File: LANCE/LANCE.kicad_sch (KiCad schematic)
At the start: 59 parts, among them J1 4s Batt, J12 Sparkmax 1 Pwr, J13 Lin Actuator 1 (Large), J15 Lasers, J16 SHT30, J17 Lin Actuator 2 (Small), J19 Sparkmax PWM 1, J2 12V, J20 Sparkmax PWM 2, J21 Sparkmax 2 Pwr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

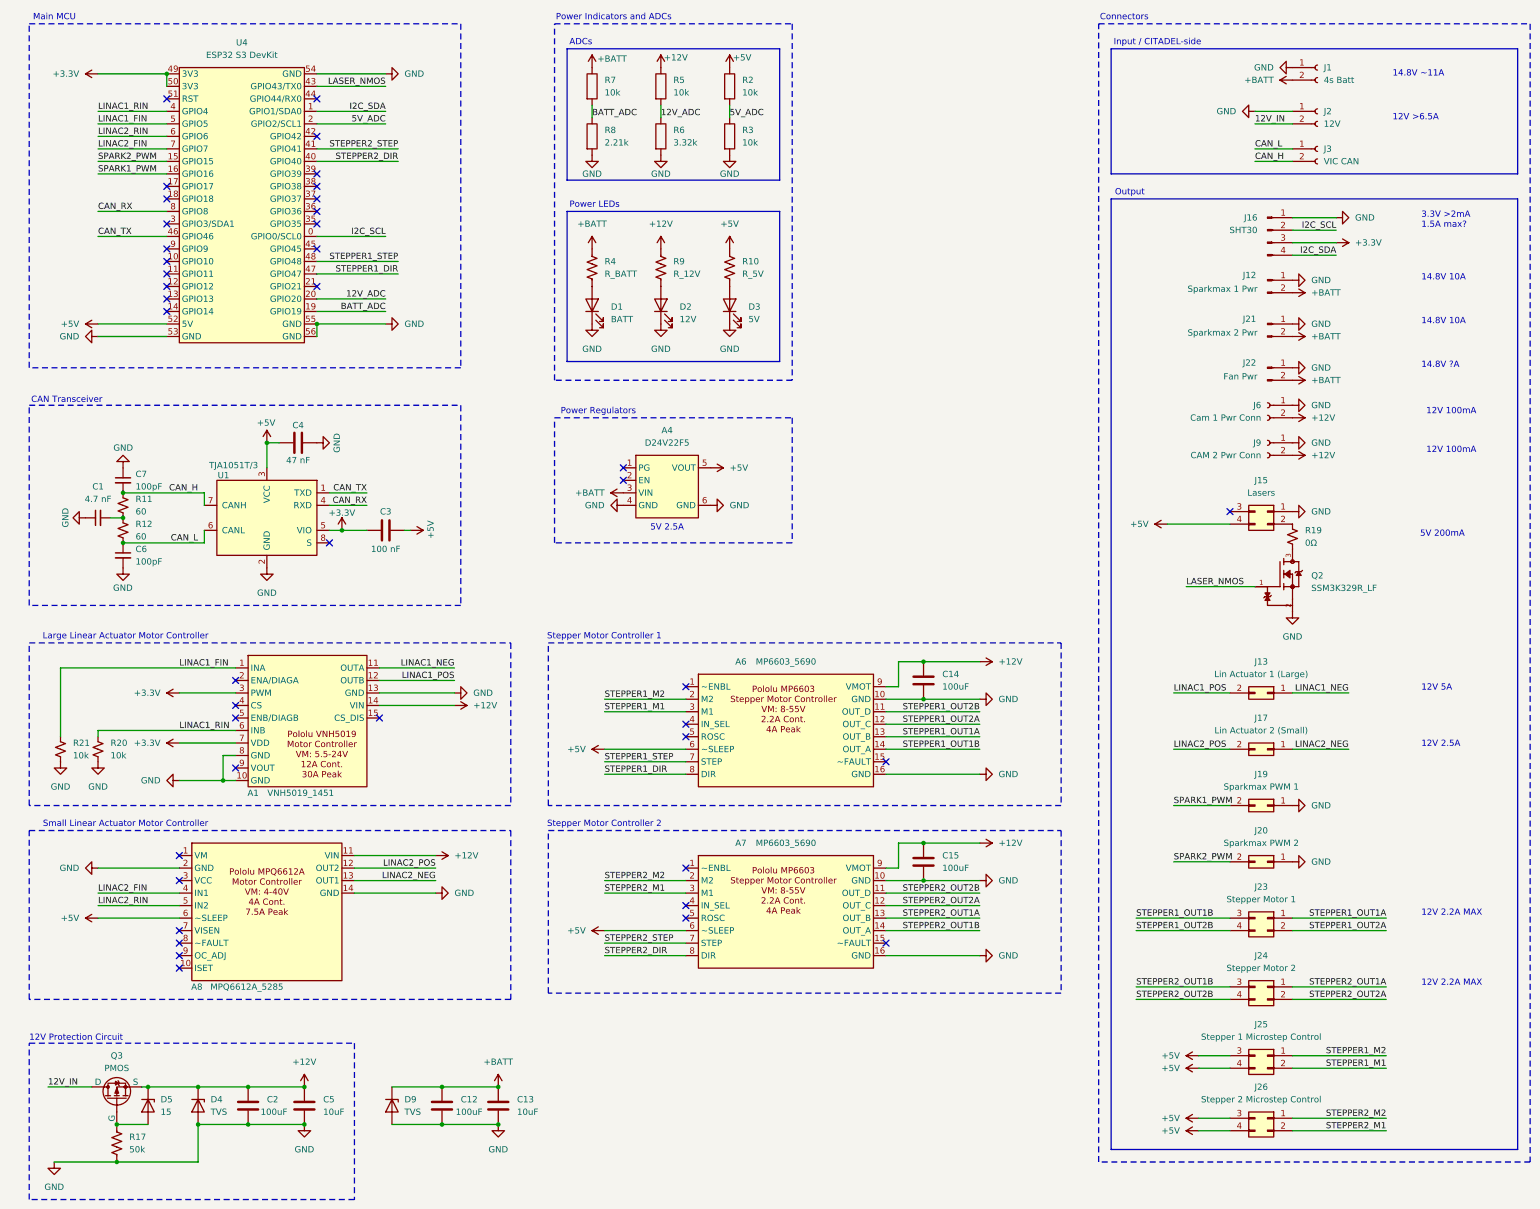
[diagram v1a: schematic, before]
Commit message: LANCE 2026 r1.02
Changed nSLEEP on MP6603 (x2) and on MPQ6612A to 3.3V, moved CAN_TX to non-strapping pin 9 on ESP32, changed SHT30 connector to I2C connector convention used on Core and Antenna, moved SHT30 connector to bottom right, rerouted 5V trace, added 63uF (x4) bank to battery trace to lessen voltage sag, grouped ground vias, and added Gerbers/Drill files
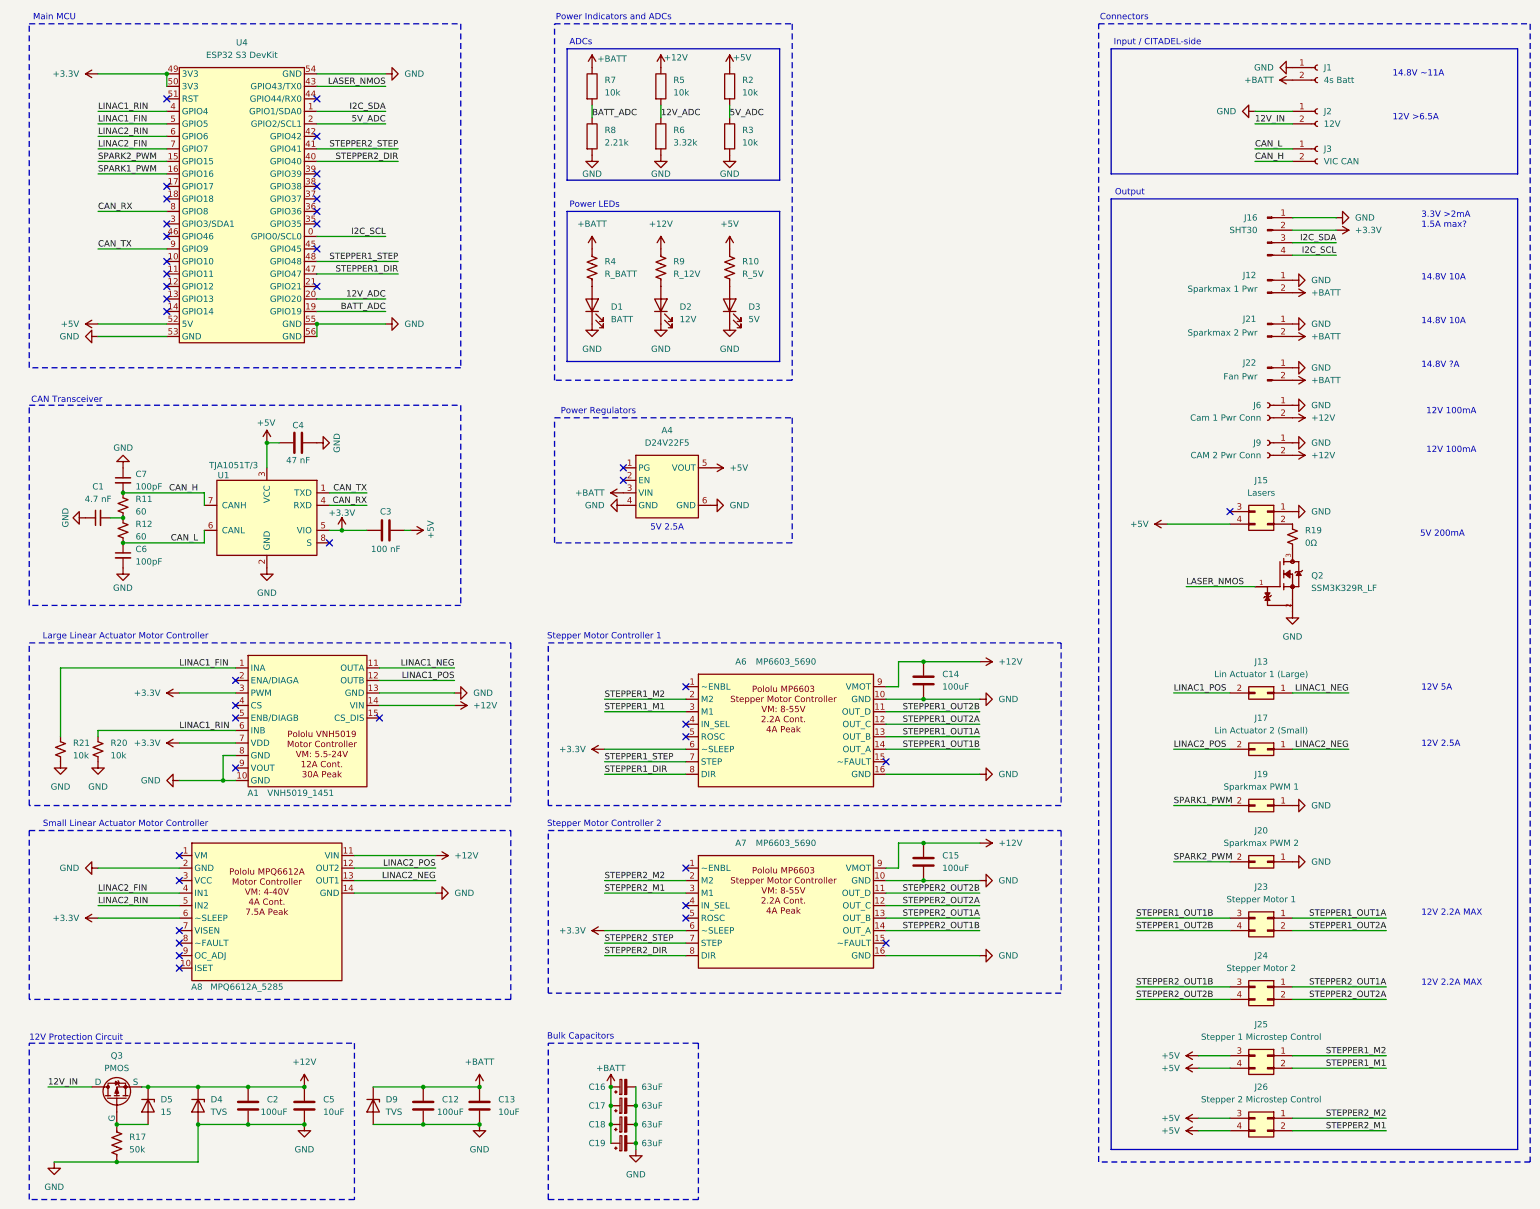
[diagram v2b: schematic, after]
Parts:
- added C16, C17, C18, C19: 63uF, Capacitor_SMD:CP_Elec_6.3x7.7, symbol Device:C_Polarized_Small
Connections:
- net +3.3V: now also A6.6 (~SLEEP), A7.6 (~SLEEP), A8.6 (~SLEEP), J16.2 (Pin_2); no longer J16.3 (Pin_3)
- net +5V: no longer A6.6 (~SLEEP), A7.6 (~SLEEP), A8.6 (~SLEEP)
- net +BATT: now also C16.1, C17.1, C18.1, C19.1
- net CAN_TX: now also U4.9 (GPIO9); no longer U4.46 (GPIO46)
- net GND: now also C16.2, C17.2, C18.2, C19.2
- net I2C_SCL: now also J16.4 (Pin_4); no longer J16.2 (Pin_2)
- net I2C_SDA: now also J16.3 (Pin_3); no longer J16.4 (Pin_4)
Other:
- note added: "Bulk Capacitors"
- moved on the sheet: C12, C13, D9
